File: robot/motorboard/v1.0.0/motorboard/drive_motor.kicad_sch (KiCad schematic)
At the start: 2 parts

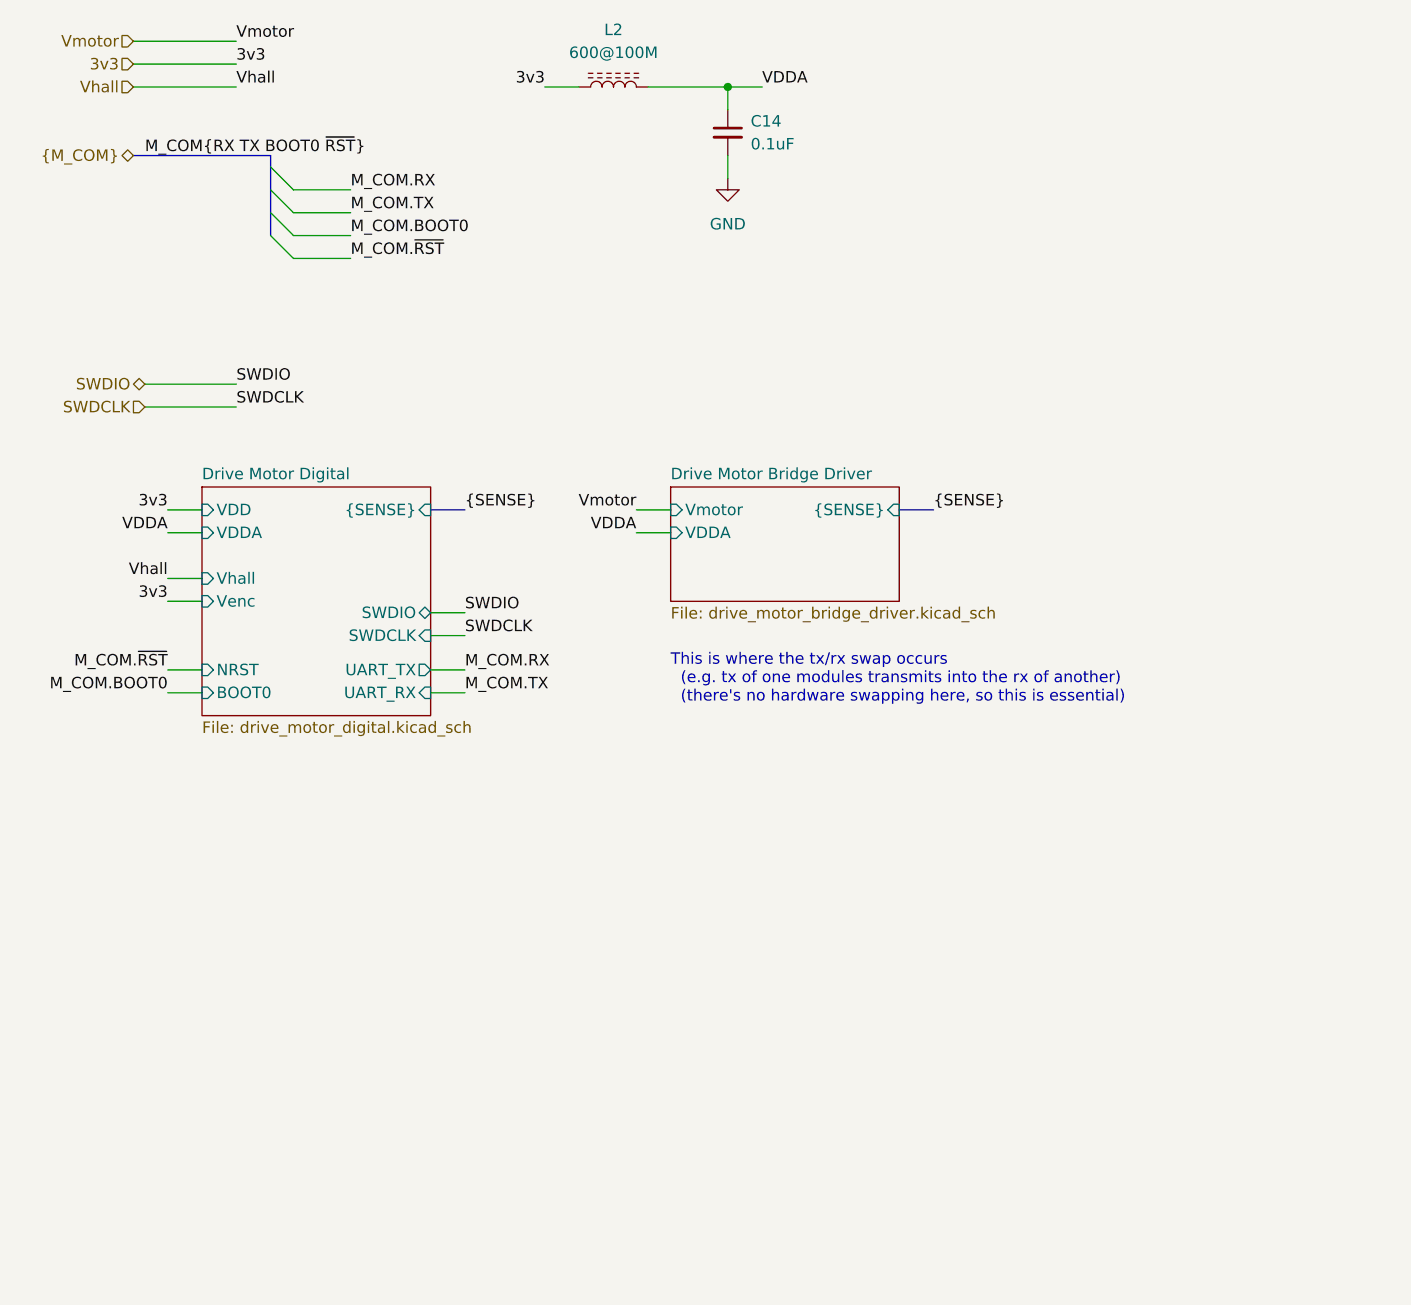
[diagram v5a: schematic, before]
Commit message: cleaned up remaining schematics
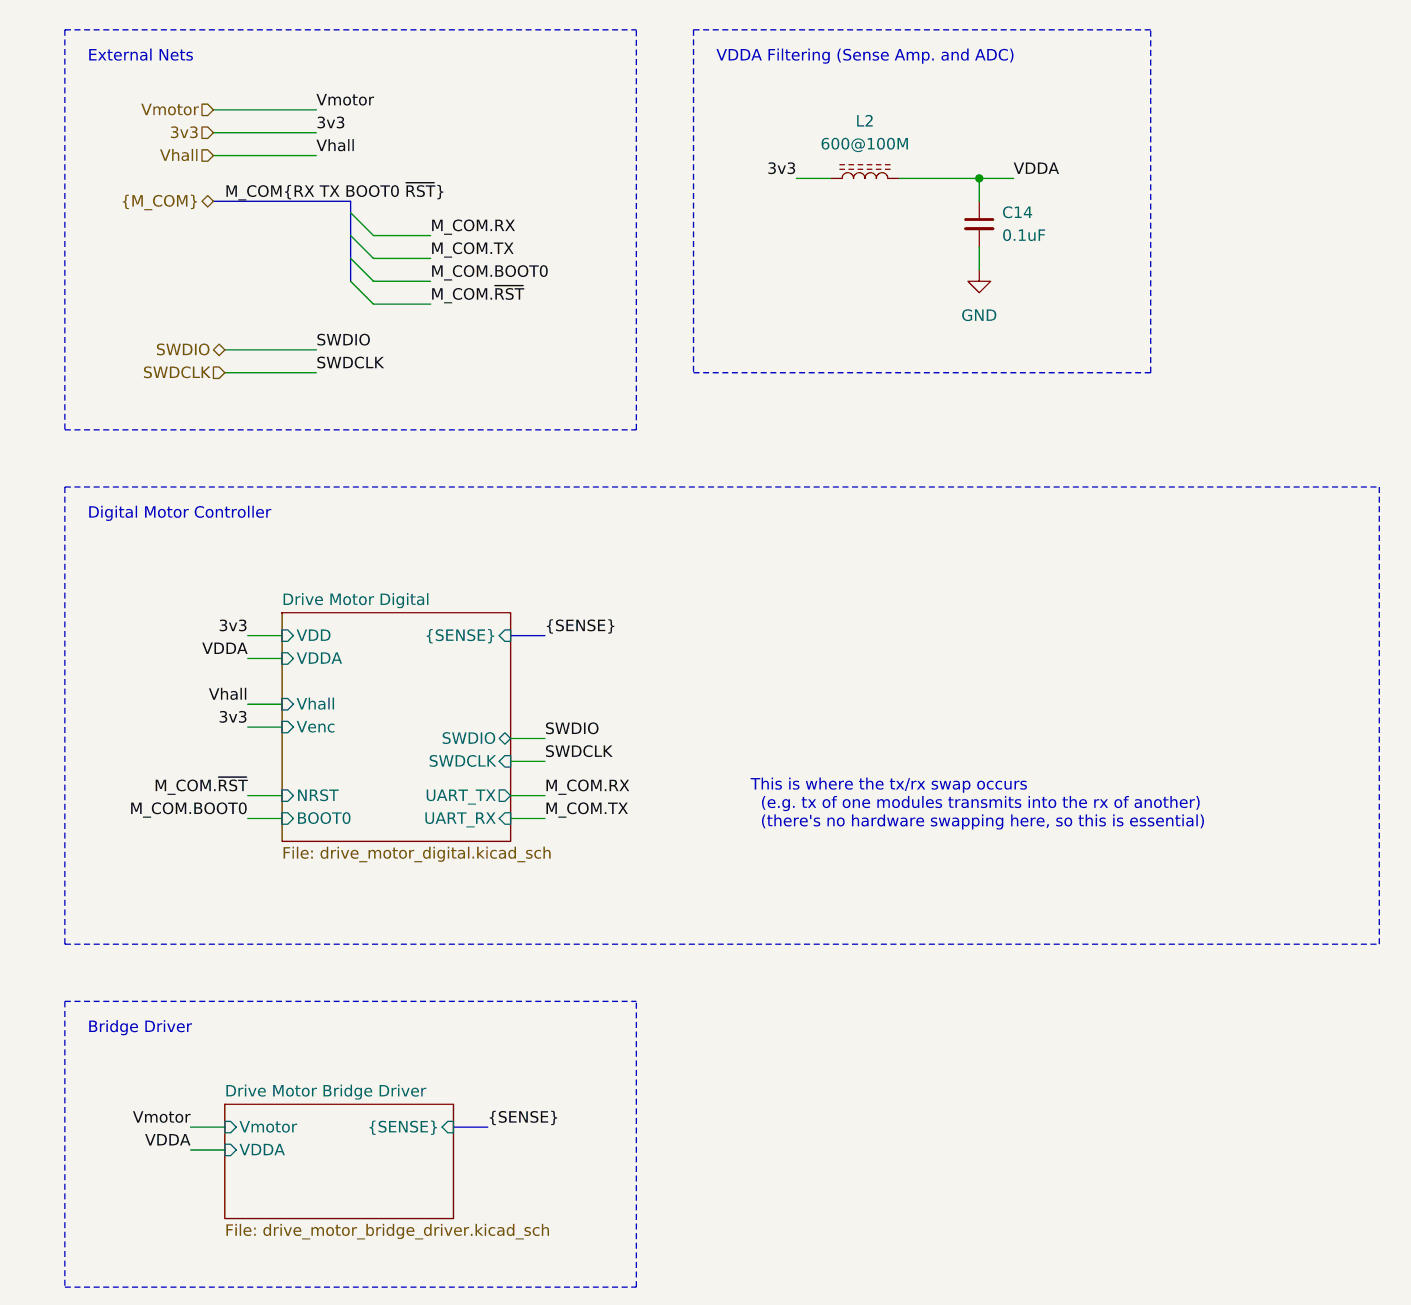
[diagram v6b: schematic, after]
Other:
- note added: "Bridge Driver"
- note added: "Digital Motor Controller"
- note added: "External Nets"
- note added: "VDDA Filtering (Sense Amp. and ADC)"
- moved on the sheet: C14, L2

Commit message: updated title block
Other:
- company: (none) -> The A-Team (RC SSL)
- title: (none) -> Motorboard
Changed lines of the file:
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@@
 (kicad_sch (version 20210621) (generator eeschema)
   (paper "A")
+  (title_block
+    (title "Motorboard")
+    (date "2021-11-14")
+    (rev "1.0.0")
+    (company "The A-Team (RC SSL)")
+    (comment 1 "Designed By: W. Stuckey & R. Osawa")
+    (comment 2 "Reviewed By:")
+  )
   (bus_alias "SENSE" (members "SENSE.U" "SENSE.V" "SENSE.W"))
   (junction (at 120.65 35.56) (diameter 0.9144) (color 0 0 0 0))

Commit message: more footprint assignments
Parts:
- L2: footprint (none) -> Inductor_SMD:L_0603_1608Metric_Pad1.05x0.95mm_HandSolder
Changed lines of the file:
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@@
   (symbol (lib_id "power:GND") (at 120.65 45.72 0)
     (in_bom yes) (on_board yes) (fields_autoplaced)
-    (property "Reference" "#PWR062" (id 0) (at 120.65 52.07 0)
+    (property "Reference" "#PWR0122" (id 0) (at 120.65 52.07 0)
       (effects (font (size 1.27 1.27)) hide)
     )
@@
     (property "Reference" "L2" (id 0) (at 107.95 29.21 90))
     (property "Value" "600@100M" (id 1) (at 107.95 31.75 90))
-    (property "Footprint" "" (id 2) (at 107.95 35.56 0)
+    (property "Footprint" "Inductor_SMD:L_0603_1608Metric_Pad1.05x0.95mm_HandSolder" (id 2) (at 107.95 35.56 0)
       (effects (font (size 1.27 1.27)) hide)
     )
